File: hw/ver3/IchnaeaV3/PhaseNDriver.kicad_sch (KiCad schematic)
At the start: 26 parts, among them Q2 MCAC80N10Y, Q3 MCAC80N10Y, U2 HIP2210

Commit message: Experiment with a new power stage layout
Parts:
- renumbered C6 to C27, C8 to C28, C4 to C29, C71 to C30, C9 to C31, C10 to C32, C11 to C33, C42 to C34, C48 to C35, C54 to C36, C60 to C37, L1 to L3, R75 to R30, R76 to R31, R5 to R32, R6 to R33, R7 to R34, TP7 to TP24, TP6 to TP25, TP9 to TP26, TP8 to TP27, TP10 to TP28, TP11 to TP29, U2 to U6

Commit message: I might've made a critical error
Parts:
- Q2, Q3: DigiKey 353-MCAC80N10Y-TPCT-ND -> (none)
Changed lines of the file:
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@@
 			)
 		)
+		(property "JLCPCB Rotation Offset" ""
+			(at 137.16 92.71 0)
+			(effects
+				(font
+					(size 1.27 1.27)
+				)
+				(hide yes)
+			)
+		)
 		(pin "1"
 		)
@@
 			)
 		)
+		(property "JLCPCB Rotation Offset" ""
+			(at 82.55 106.68 0)
+			(effects
+				(font
+					(size 1.27 1.27)
+				)
+				(hide yes)
+			)
+		)
 		(pin "2"
 		)
@@
 			)
 		)
+		(property "JLCPCB Rotation Offset" ""
+			(at 166.37 76.2 0)
+			(effects
+				(font
+					(size 1.27 1.27)
+				)
+				(hide yes)
+			)
+		)
 		(pin "2"
 		)
@@
 			)
 		)
+		(property "JLCPCB Rotation Offset" ""
+			(at 71.12 92.71 0)
+			(effects
+				(font
+					(size 1.27 1.27)
+				)
+				(hide yes)
+			)
+		)
 		(pin "1"
 		)
@@
 			)
 		)
+		(property "JLCPCB Rotation Offset" ""
+			(at 209.55 105.41 0)
+			(effects
+				(font
+					(size 1.27 1.27)
+				)
+				(hide yes)
+			)
+		)
 		(pin "1"
 		)
@@
 			)
 		)
+		(property "JLCPCB Rotation Offset" ""
+			(at 173.99 99.06 0)
+			(effects
+				(font
+					(size 1.27 1.27)
+				)
+				(hide yes)
+			)
+		)
 		(pin "1"
 		)
@@
 			)
 		)
+		(property "JLCPCB Rotation Offset" ""
+			(at 64.77 99.06 0)
+			(effects
+				(font
+					(size 1.27 1.27)
+				)
+				(hide yes)
+			)
+		)
 		(pin "1"
 		)
@@
 			)
 		)
+		(property "JLCPCB Rotation Offset" ""
+			(at 175.26 81.28 0)
+			(effects
+				(font
+					(size 1.27 1.27)
+				)
+				(hide yes)
+			)
+		)
 		(pin "1"
 		)
@@
 			)
 		)
-		(property "DigiKey" "353-MCAC80N10Y-TPCT-ND"
+		(property "JLCPCB Rotation Offset" ""
 			(at 119.38 105.41 0)
 			(effects
@@
 			)
 		)
+		(property "JLCPCB Rotation Offset" ""
+			(at 198.12 105.41 0)
+			(effects
+				(font
+					(size 1.27 1.27)
+				)
+				(hide yes)
+			)
+		)
 		(pin "1"
 		)
@@
 			)
 		)
+		(property "JLCPCB Rotation Offset" ""
+			(at 63.5 83.82 0)
+			(effects
+				(font
+					(size 1.27 1.27)
+				)
+				(hide yes)
+			)
+		)
 		(pin "1"
 		)
@@
 			)
 		)
+		(property "JLCPCB Rotation Offset" ""
+			(at 111.76 113.03 0)
+			(effects
+				(font
+					(size 1.27 1.27)
+				)
+				(hide yes)
+			)
+		)
 		(pin "1"
 		)
@@
 			)
 		)
-		(property "DigiKey" "353-MCAC80N10Y-TPCT-ND"
+		(property "DigiKey" ""
+			(at 119.38 92.71 0)
+			(effects
+				(font
+					(size 1.27 1.27)
+				)
+				(hide yes)
+			)
+		)
+		(property "JLCPCB Rotation Offset" ""
 			(at 119.38 92.71 0)
 			(effects
@@
 			)
 		)
+		(property "JLCPCB Rotation Offset" ""
+			(at 76.2 100.33 0)
+			(effects
+				(font
+					(size 1.27 1.27)
+				)
+				(hide yes)
+			)
+		)
 		(pin "1"
 		)
@@
 			)
 		)
+		(property "JLCPCB Rotation Offset" ""
+			(at 186.69 105.41 0)
+			(effects
+				(font
+					(size 1.27 1.27)
+				)
+				(hide yes)
+			)
+		)
 		(pin "1"
 		)
@@
 			)
 		)
+		(property "JLCPCB Rotation Offset" ""
+			(at 106.68 95.25 0)
+			(effects
+				(font
+					(size 1.27 1.27)
+				)
+				(hide yes)
+			)
+		)
 		(pin "1"
 		)
@@
 			)
 		)
+		(property "JLCPCB Rotation Offset" ""
+			(at 111.76 107.95 0)
+			(effects
+				(font
+					(size 1.27 1.27)
+				)
+				(hide yes)
+			)
+		)
 		(pin "1"
 		)
@@
 			)
 		)
+		(property "JLCPCB Rotation Offset" ""
+			(at 186.69 66.04 0)
+			(effects
+				(font
+					(size 1.27 1.27)
+				)
+				(hide yes)
+			)
+		)
 		(pin "1"
 		)
@@
 			)
 		)
+		(property "JLCPCB Rotation Offset" ""
+			(at 175.26 71.12 0)
+			(effects
+				(font
+					(size 1.27 1.27)
+				)
+				(hide yes)
+			)
+		)
 		(pin "1"
 		)
@@
 			)
 		)
+		(property "JLCPCB Rotation Offset" ""
+			(at 161.29 86.36 0)
+			(effects
+				(font
+					(size 1.27 1.27)
+				)
+				(hide yes)
+			)
+		)
 		(pin "1"
 		)
@@
 			)
 		)
+		(property "JLCPCB Rotation Offset" ""
+			(at 220.98 105.41 0)
+			(effects
+				(font
+					(size 1.27 1.27)
+				)
+				(hide yes)
+			)
+		)
 		(pin "1"
 		)
@@
 			)
 		)
+		(property "JLCPCB Rotation Offset" ""
+			(at 111.76 101.6 0)
+			(effects
+				(font
+					(size 1.27 1.27)
+				)
+				(hide yes)
+			)
+		)
 		(pin "1"
 		)
@@
 			)
 		)
+		(property "JLCPCB Rotation Offset" ""
+			(at 66.04 77.47 0)
+			(effects
+				(font
+					(size 1.27 1.27)
+				)
+				(hide yes)
+			)
+		)
 		(pin "1"
 		)
@@
 			)
 		)
+		(property "JLCPCB Rotation Offset" ""
+			(at 232.41 105.41 0)
+			(effects
+				(font
+					(size 1.27 1.27)
+				)
+				(hide yes)
+			)
+		)
 		(pin "1"
 		)
@@
 			)
 		)
+		(property "JLCPCB Rotation Offset" ""
+			(at 95.25 99.06 0)
+			(effects
+				(font
+					(size 1.27 1.27)
+				)
+				(hide yes)
+			)
+		)
 		(pin "2"
 		)
@@
 			(at 128.27 92.71 0)
 			(effects
+				(font
+					(size 1.27 1.27)
+				)
+				(hide yes)
+			)
+		)
+		(property "JLCPCB Rotation Offset" ""
+			(at 128.27 92.71 0)
+			(effects

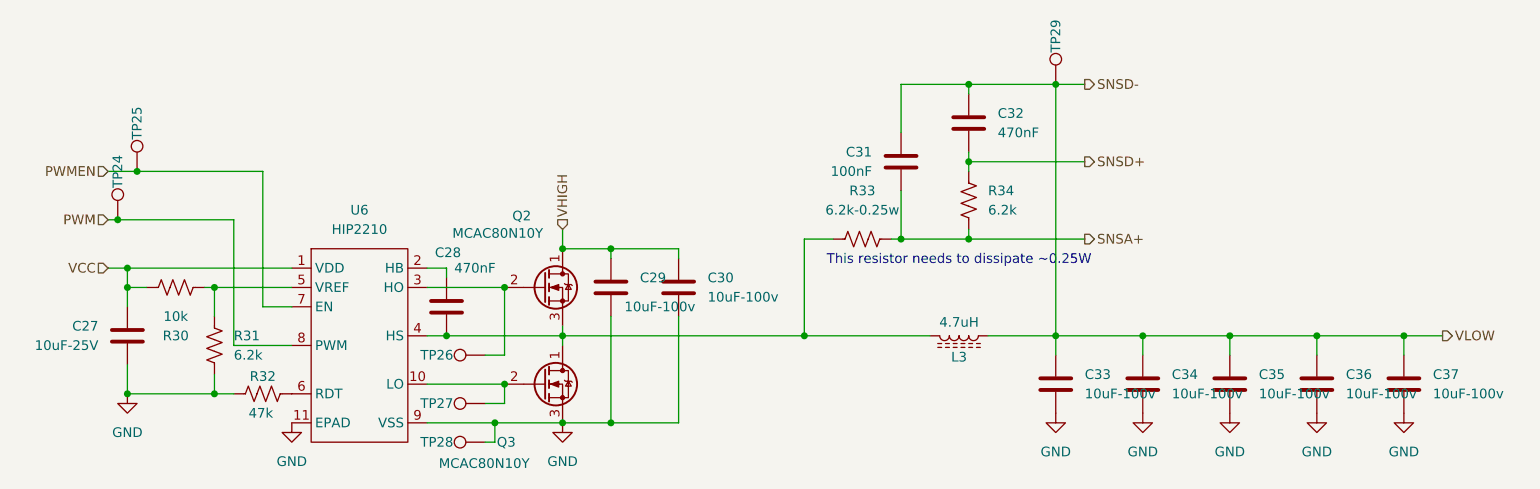
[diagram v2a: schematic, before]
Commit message: Improve more of the power stage layout
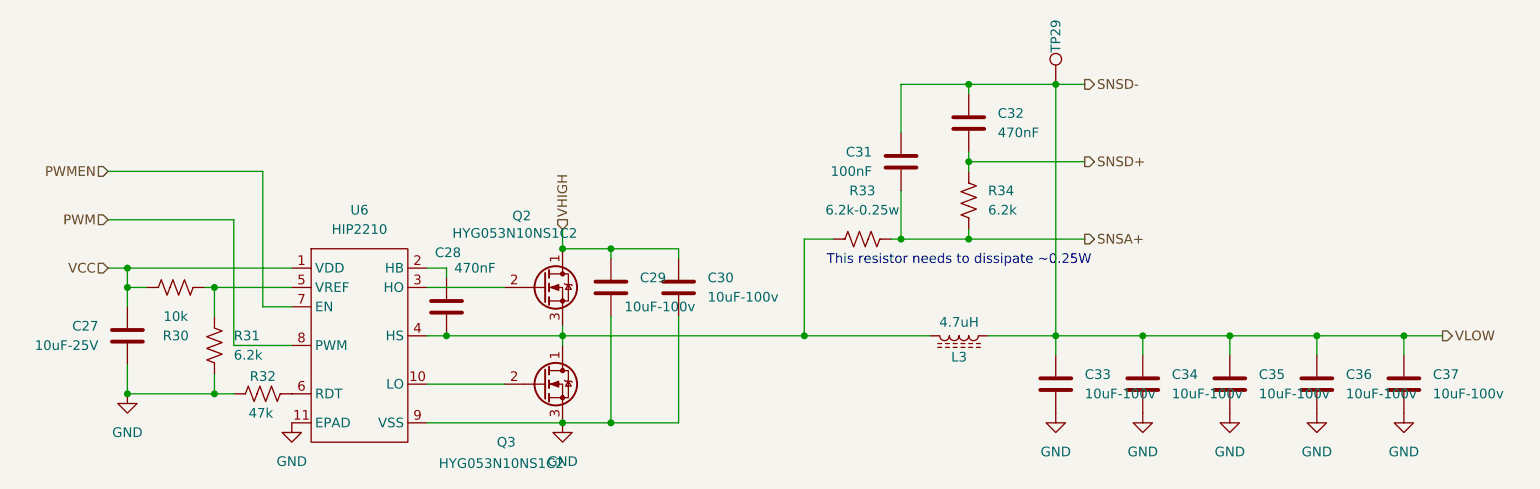
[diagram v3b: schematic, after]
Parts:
- removed TP24, TP25, TP26, TP27, TP28: TestPoint, TestPoint:TestPoint_Pad_D1.0mm, symbol Connector:TestPoint
- Q2, Q3: value MCAC80N10Y -> HYG053N10NS1C2; Digikey 353-MCAC80N10Y-TPCT-ND -> N/A; LCSC N/A -> C2986239

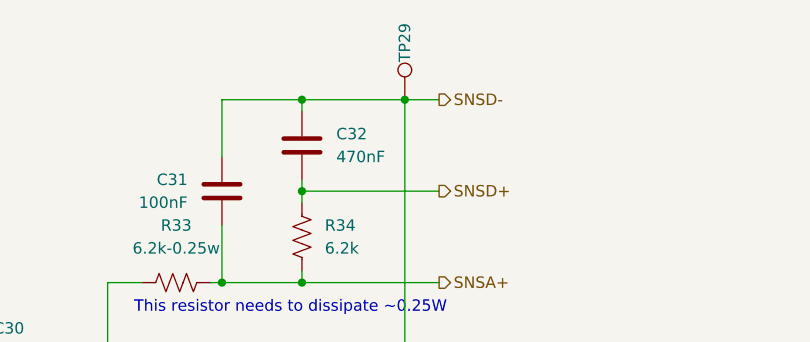
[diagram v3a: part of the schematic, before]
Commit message: Start rework of power stage layout to shorten inductive path and increase current handling
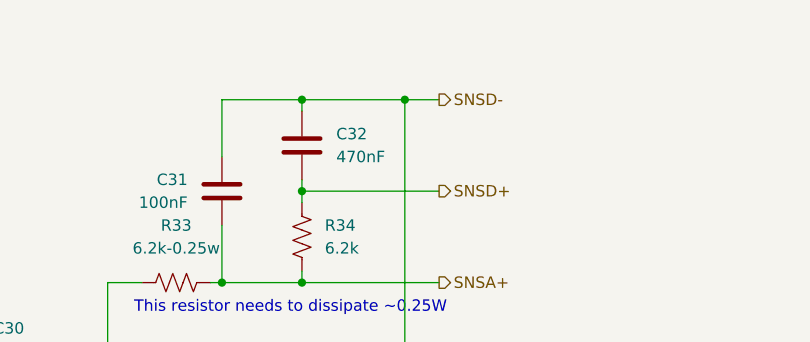
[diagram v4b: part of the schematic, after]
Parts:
- removed TP29: TestPoint, TestPoint:TestPoint_Pad_D1.0mm, symbol Connector:TestPoint
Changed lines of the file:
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@@
-	)
-	(symbol
-		(lib_id "Connector:TestPoint")
-		(at 186.69 66.04 0)
-		(unit 1)
-		(exclude_from_sim no)
-		(in_bom yes)
-		(on_board yes)
-		(dnp no)
-		(property "Reference" "TP29"
-			(at 186.69 59.69 90)
-			(effects
-				(font
-					(size 1.27 1.27)
-				)
-			)
-		)
-		(property "Value" "TestPoint"
-			(at 189.23 62.738 90)
-			(effects
-				(font
-					(size 1.27 1.27)
-				)
-				(hide yes)
-			)
-		)
-		(property "Footprint" "TestPoint:TestPoint_Pad_D1.0mm"
-			(at 191.77 66.04 0)
-			(effects
-				(font
-					(size 1.27 1.27)
-				)
-				(hide yes)
-			)
-		)
-		(property "Datasheet" "~"
-			(at 191.77 66.04 0)
-			(effects
-				(font
-					(size 1.27 1.27)
-				)
-				(hide yes)
-			)
-		)
-		(property "Description" "test point"
-			(at 186.69 66.04 0)
-			(effects
-				(font
-					(size 1.27 1.27)
-				)
-				(hide yes)
-			)
-		)
-		(property "LCSC" "N/A"
-			(at 186.69 66.04 0)
-			(effects
-				(font
-					(size 1.27 1.27)
-				)
-				(hide yes)
-			)
-		)
-		(property "JLCPCB Rotation Offset" ""
-			(at 186.69 66.04 0)
-			(effects
-				(font
-					(size 1.27 1.27)
-				)
-				(hide yes)
-			)
-		)
-		(property "DigiKey" ""
-			(at 186.69 66.04 0)
-			(effects
-				(font
-					(size 1.27 1.27)
-				)
-				(hide yes)
-			)
-		)
-		(pin "1"
-		)
-		(instances
-			(project "IchnaeaV3"
-				(path "/93408532-1ffa-463d-873c-16289d2b7987/31a930eb-86fc-490d-aa2b-31b72c4dd29d/171364aa-6f2d-4723-9ce2-aacc140a6e7a"
-					(reference "TP29")
-					(unit 1)
-				)
-				(path "/93408532-1ffa-463d-873c-16289d2b7987/31a930eb-86fc-490d-aa2b-31b72c4dd29d/acf0bc45-d506-42ae-8f5d-490b1286e5e0"
-					(reference "TP35")
-					(unit 1)
-				)
-				(path "/93408532-1ffa-463d-873c-16289d2b7987/31a930eb-86fc-490d-aa2b-31b72c4dd29d/48047d75-e488-4da1-b4d9-5027f5fb8795"
-					(reference "TP41")
-					(unit 1)
-				)
-				(path "/93408532-1ffa-463d-873c-16289d2b7987/31a930eb-86fc-490d-aa2b-31b72c4dd29d/ed7af46d-5b91-411b-a953-18bebafe1a87"
-					(reference "TP47")
-					(unit 1)
-				)
-				(path "/93408532-1ffa-463d-873c-16289d2b7987/31a930eb-86fc-490d-aa2b-31b72c4dd29d/54a63e50-1efe-4308-b876-98aee26e8c6e"
-					(reference "TP53")
-					(unit 1)
-				)
-				(path "/93408532-1ffa-463d-873c-16289d2b7987/31a930eb-86fc-490d-aa2b-31b72c4dd29d/d7eacb53-72cb-4ae3-a7a6-7938b9062ae2"
-					(reference "TP59")
-					(unit 1)
-				)
-			)
-		)
 	)
 	(symbol
